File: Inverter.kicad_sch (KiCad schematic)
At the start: 47 parts, among them IC1 STGIPQ3H60T-HL, IC2 ACS724LLCTR-05AU-T

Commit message: update description & value
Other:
- note added: "CF = 1nF CBypass = 0.1 uF"
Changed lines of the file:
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@@
     (effects (font (size 1.27 1.27) bold) (justify left bottom))
   )
-  (text "ACS VCC \nSupply = 6V\n" (at 285.75 64.135 0)
-    (effects (font (size 1.5 1.5) (thickness 0.254) bold) (justify left bottom))
+  (text "ACS VCC Supply = 6V\n" (at 299.085 64.77 0)
+    (effects (font (size 1.27 1.27) (thickness 0.254) bold) (justify left bottom))
   )
   (text "R_SD is a pull-up resistor to prevent floating logic. \nValue: 1k or 2.2 k for 3.3V or 5V MCU supply\n"
@@
     (effects (font (size 1.27 1.27) (thickness 0.4) bold) (justify left bottom))
   )
+  (text "CF = 1nF\nCBypass = 0.1 uF" (at 299.085 69.85 0)
+    (effects (font (size 1.27 1.27) (thickness 0.254) bold) (justify left bottom))
+  )
   (text "Rsf, Csf used to prevent \nprotection circuit malfunction"

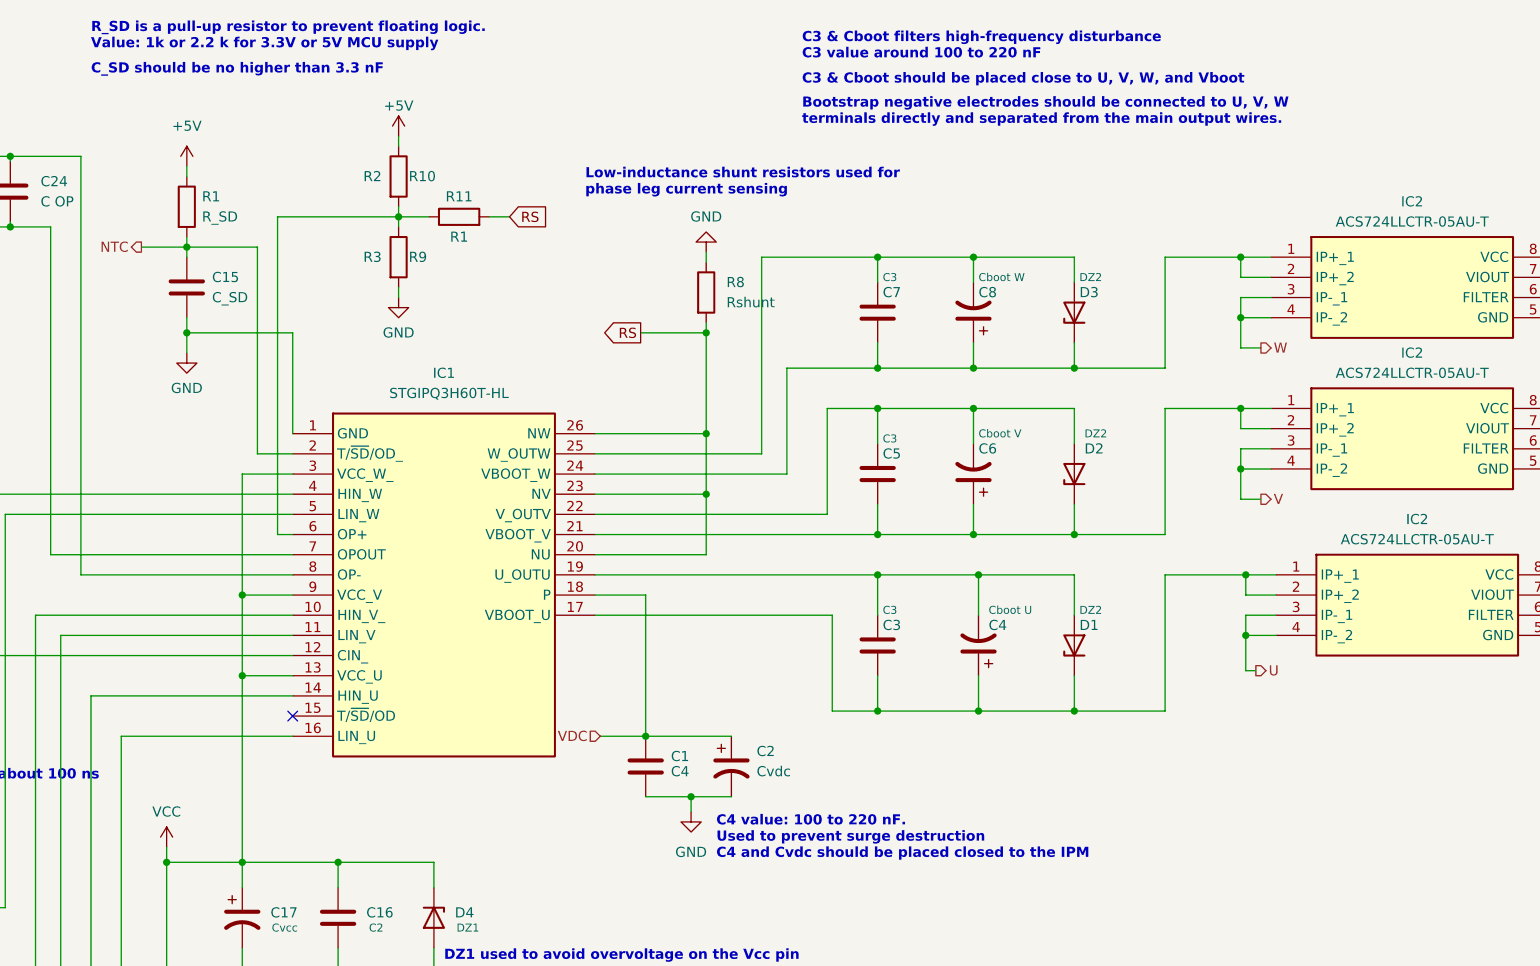
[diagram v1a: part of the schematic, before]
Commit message: update power supply page
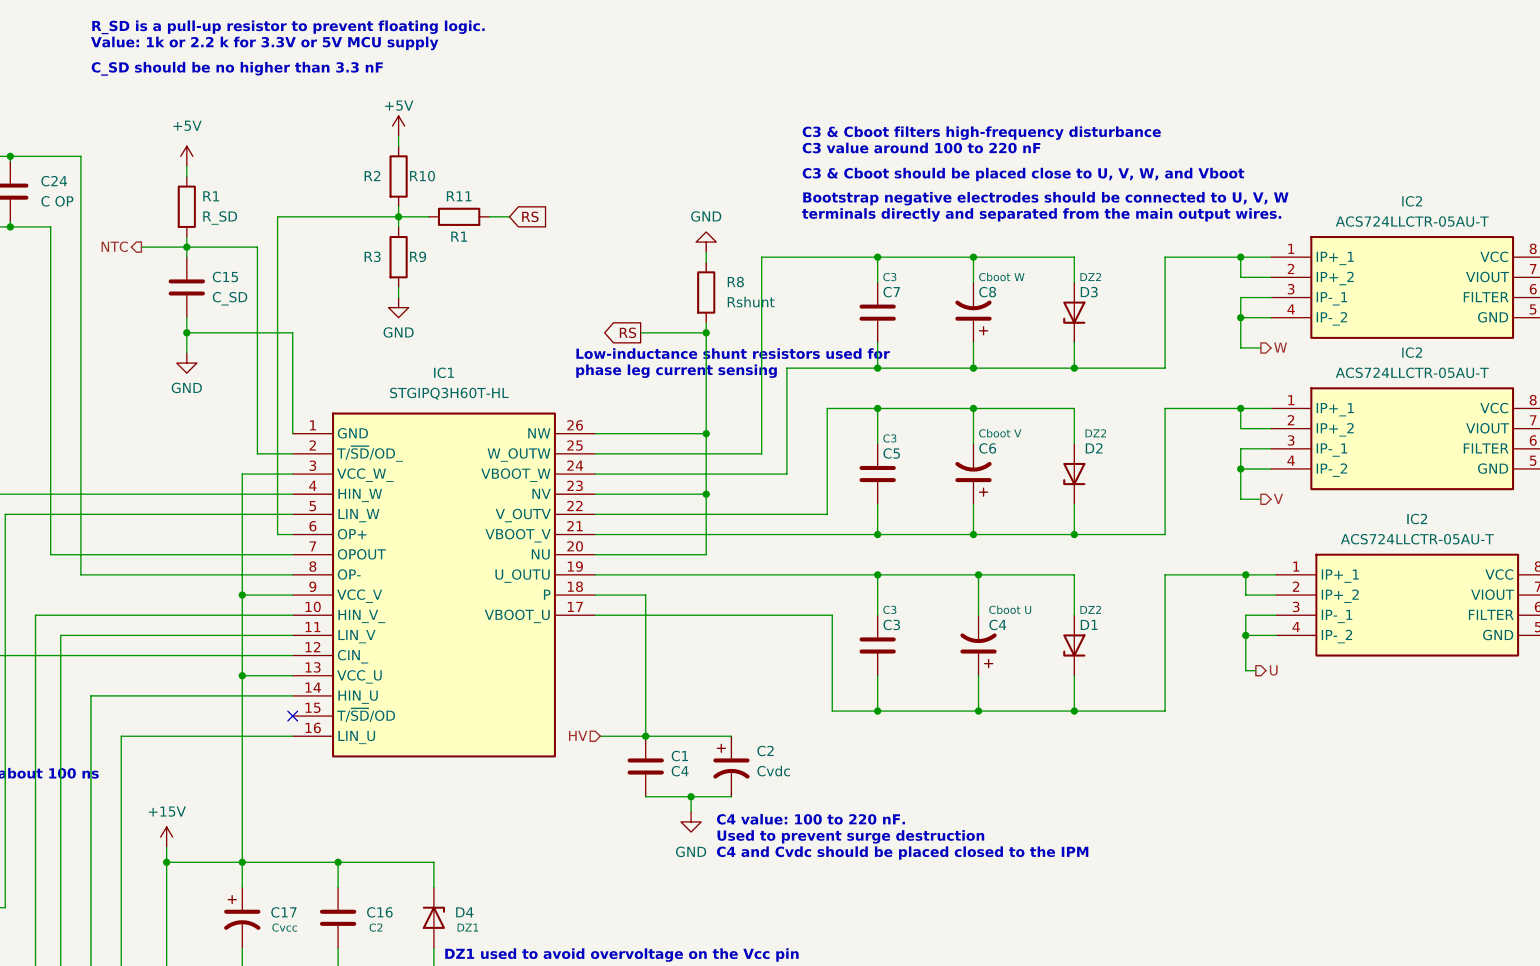
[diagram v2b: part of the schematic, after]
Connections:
- net GND renamed +15V
- net VDC renamed HV
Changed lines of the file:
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@@
   )
   (text "C3 & Cboot should be placed close to U, V, W, and Vboot"
-    (at 159.385 21.59 0)
+    (at 159.385 33.655 0)
     (effects (font (size 1.27 1.27) bold) (justify left bottom))
   )
@@
   )
   (text "Bootstrap negative electrodes should be connected to U, V, W\nterminals directly and separated from the main output wires."
-    (at 159.385 26.67 0)
+    (at 159.385 38.735 0)
     (effects (font (size 1.27 1.27) bold) (justify left bottom))
   )
@@
   )
   (text "C3 & Cboot filters high-frequency disturbance\nC3 value around 100 to 220 nF"
-    (at 159.385 18.415 0)
+    (at 159.385 30.48 0)
     (effects (font (size 1.27 1.27) bold) (justify left bottom))
   )
@@
   )
   (text "Low-inductance shunt resistors used for \nphase leg current sensing"
-    (at 132.08 35.56 0)
+    (at 130.81 58.42 0)
     (effects (font (size 1.27 1.27) bold) (justify left bottom))
   )
@@
     (effects (font (size 1.27 1.27)) (justify left))
   )
-  (hierarchical_label "VDC" (shape input) (at 133.985 103.505 180) (fields_autoplaced)
+  (hierarchical_label "HV" (shape input) (at 133.985 103.505 180) (fields_autoplaced)
     (effects (font (size 1.27 1.27)) (justify right))
   )
@@
         (path "/c97a22ab-71f8-4b91-b313-15b8a3e640d7/fb44c483-375e-43d2-9d1e-806996239436"
           (reference "#PWR021") (unit 1)
+        )
+      )
+    )
+  )
+  (symbol (lib_id "power:+15V") (at 79.375 117.475 0) (unit 1)
+    (in_bom yes) (on_board yes) (dnp no) (fields_autoplaced)
+    (property "Reference" "#PWR019" (at 79.375 121.285 0)
+      (effects (font (size 1.27 1.27)) hide)
+    )
+    (property "Value" "+15V" (at 79.375 113.03 0)
+      (effects (font (size 1.27 1.27)))
+    )
+    (property "Footprint" "" (at 79.375 117.475 0)
+      (effects (font (size 1.27 1.27)) hide)
+    )
+    (property "Datasheet" "" (at 79.375 117.475 0)
+      (effects (font (size 1.27 1.27)) hide)
+    )
+    (pin "1")
+    (instances
+      (project "Main"
+        (path "/c97a22ab-71f8-4b91-b313-15b8a3e640d7/fb44c483-375e-43d2-9d1e-806996239436"
+          (reference "#PWR019") (unit 1)
         )
       )
@@
         )
       )
-    )
-  )
-  (symbol (lib_id "power:VCC") (at 79.375 117.475 0) (unit 1)
-    (in_bom yes) (on_board yes) (dnp no) (fields_autoplaced)
-    (property "Reference" "#PWR019" (at 79.375 121.285 0)
-      (effects (font (size 1.27 1.27)) hide)
-    )
-    (property "Value" "VCC" (at 79.375 113.03 0)
-      (effects (font (size 1.27 1.27)))
-    )
-    (property "Footprint" "" (at 79.375 117.475 0)
-      (effects (font (size 1.27 1.27)) hide)
-    )
-    (property "Datasheet" "" (at 79.375 117.475 0)
-      (effects (font (size 1.27 1.27)) hide)
-    )
-    (pin "1")
-    (instances
-      (project "Main"
-        (path "/c97a22ab-71f8-4b91-b313-15b8a3e640d7/fb44c483-375e-43d2-9d1e-806996239436"
-          (reference "#PWR019") (unit 1)
-        )
-      )

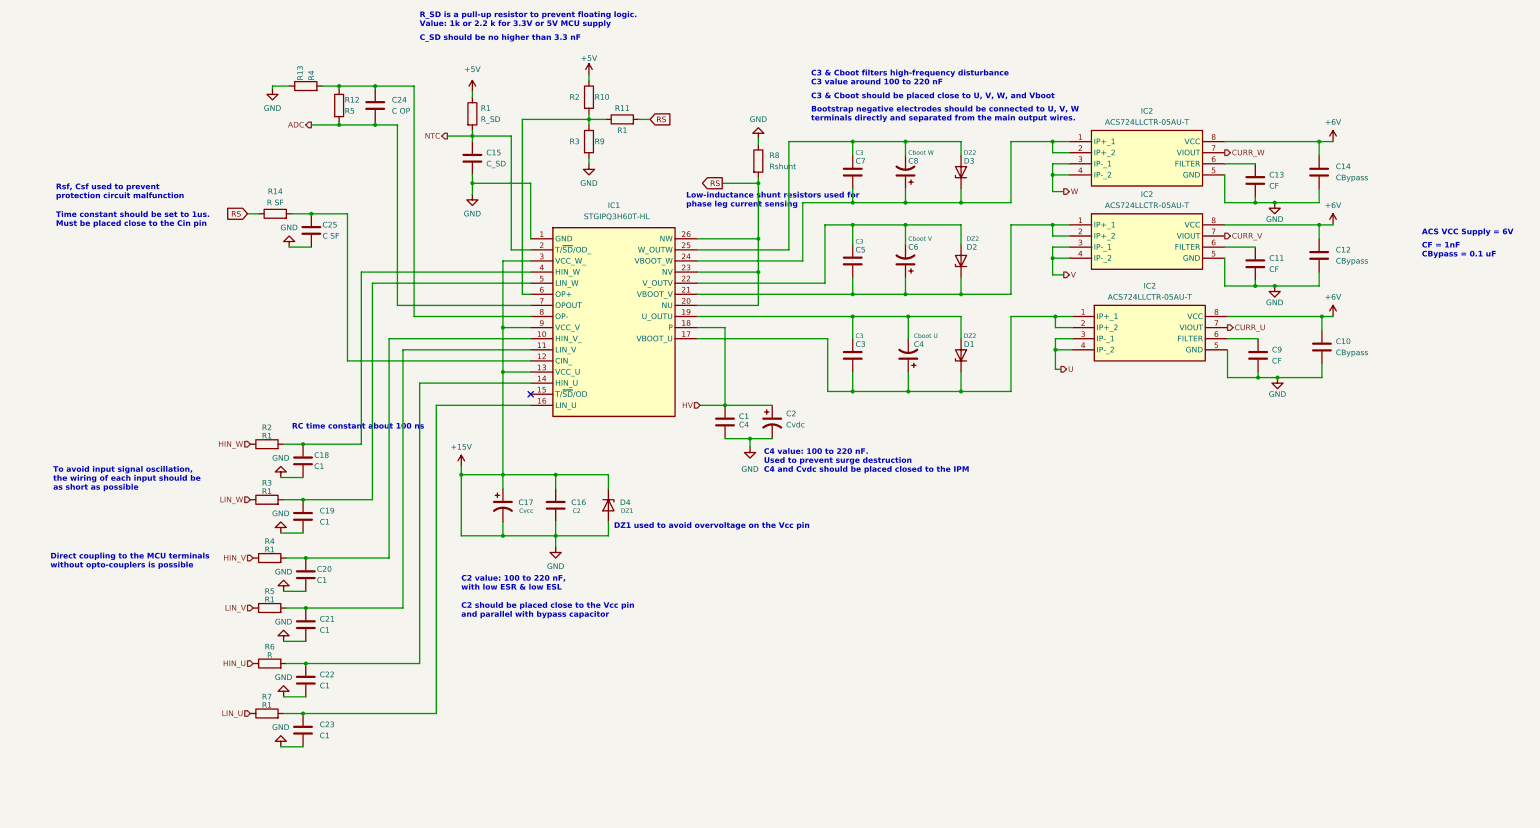
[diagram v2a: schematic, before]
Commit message: update power label
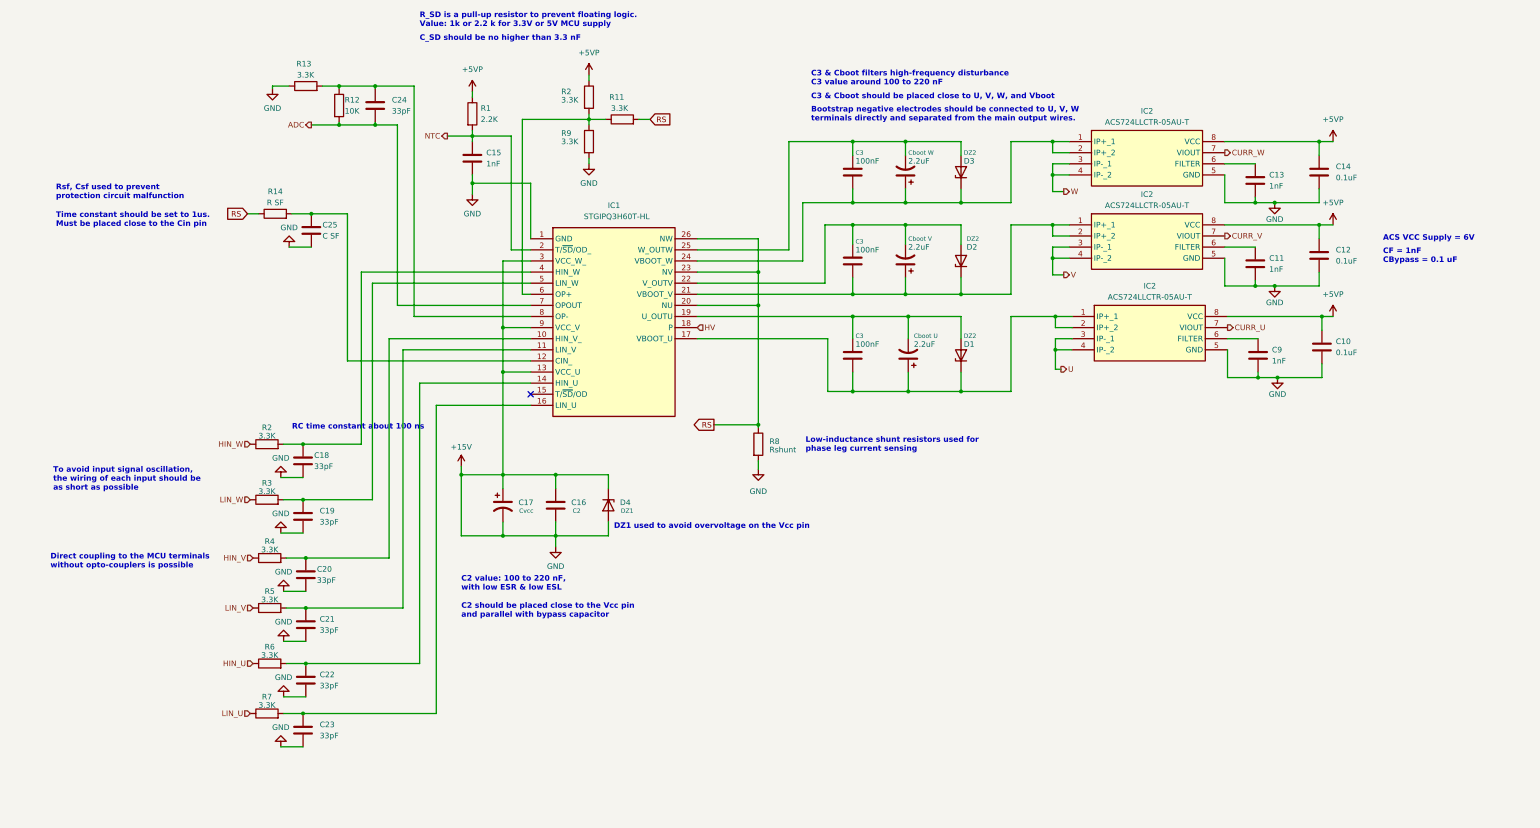
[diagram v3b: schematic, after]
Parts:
- removed C1: C4, symbol Device:C
- removed C2: Cvdc, symbol Device:C_Polarized_US
- C10, C12, C14: value CBypass -> 0.1uF
- C11, C13, C9: value CF -> 1nF
- C15: value C_SD -> 1nF
- C18, C19, C20, C21, C22, C23: value C1 -> 33pF
- C24: value C OP -> 33pF
- C3: value C3 -> 100nF
- R1: value R_SD -> 2.2K
- R11, R2, R3, R4, R5, R7: value R1 -> 3.3K
- R12: value R5 -> 10K
- R13: value R4 -> 3.3K
- R6: value R -> 3.3K
- R9: value R3 -> 3.3K
- renumbered C5 to 100nF, C7 to 100nF, C4 to 2.2uF, C6 to 2.2uF, C8 to 2.2uF, R10 to 3.3K
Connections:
- net +6V is gone; now on net +5VP: C10.2, C12.2, C14.2, IC2.8 (VCC), IC2.8 (VCC), IC2.8 (VCC)
- net +15V: now also R8.2; no longer R8.1
- net RS: now also R8.1; no longer R8.2
- net +5V renamed +5VP
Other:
- note removed: "C4 value: 100 to 220 nF. Used to prevent surge destruction C4 and Cvdc should be placed closed to the IPM"
- moved on the sheet: R8

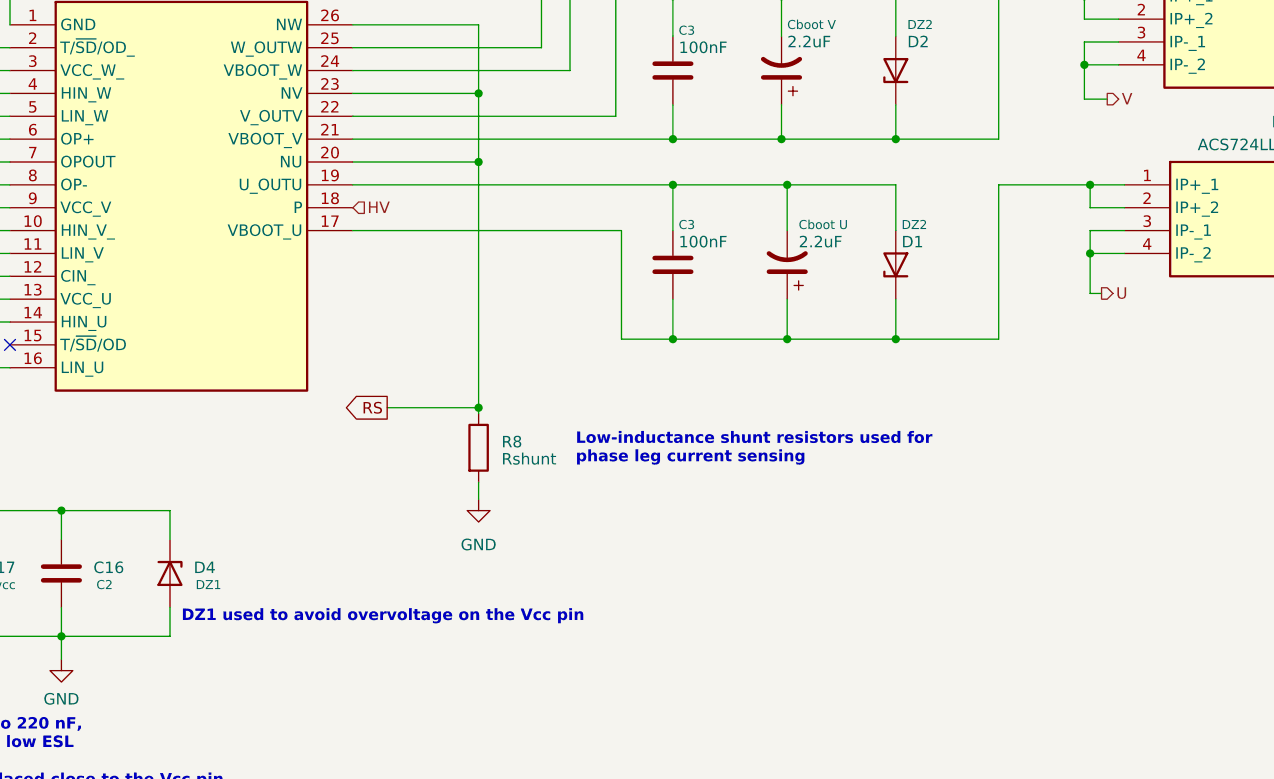
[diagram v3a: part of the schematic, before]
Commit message: adding high speed isolator
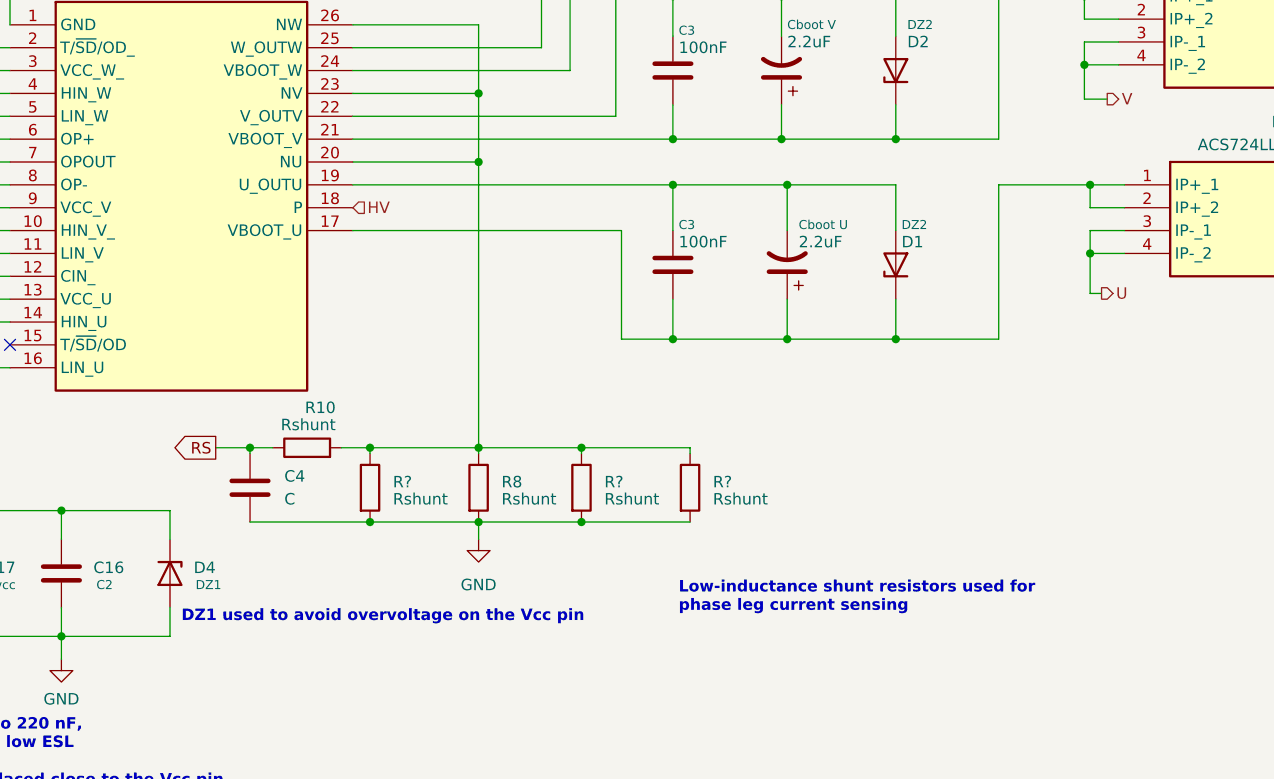
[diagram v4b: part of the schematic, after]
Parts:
- added C4: C, symbol Device:C
- added R10, R? (x3): Rshunt, symbol Device:R
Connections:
- net +15V: now also C4.2, R?.2, R?.2, R?.2
- net RS: now also C4.1, R10.1; no longer IC1.20 (NU), IC1.23 (NV), IC1.26 (NW), R8.1
- new net: IC1.20 (NU), IC1.23 (NV), IC1.26 (NW), R10.2, R8.1, R?.1, R?.1, R?.1
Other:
- moved on the sheet: R8
